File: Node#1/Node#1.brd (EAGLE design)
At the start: 100 x 80 mm, 110 parts, among them U1 BLUENRG-232, U2 SEMTECH_SX1503I091TRTSEMTECH_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, U3 MIC4468YWM, U4 LM339ADR, X1 2081-1228, X2 2081-1228, X3 2081-1228, Y1 ECS-160-12-36-AGN-TR, Y2 NX2012SA-32.768K-STD-MUB-1

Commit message: Update LBR
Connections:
- removed net N$83: X3.L2, X3.L4, X3.L6, X3.L8
- new net AGND: U$1.3, U$2.3, U$7.3, U$8.3, U3.7
- new net V+: U3.14, X3.L2, X3.L4, X3.L6, X3.L8
- net GND: no longer U$1.3, U$2.3, U$7.3, U$8.3, U3.7
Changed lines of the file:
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@@
 <contactref element="LED16" pad="K"/>
 <contactref element="D9" pad="3"/>
-<contactref element="U3" pad="7"/>
-<contactref element="U$1" pad="3"/>
-<contactref element="U$8" pad="3"/>
-<contactref element="U$7" pad="3"/>
-<contactref element="U$2" pad="3"/>
 <wire x1="-65.475" y1="-181.54" x2="-63.5" y2="-180.34" width="0" layer="19" extent="1-1"/>
 <wire x1="-61.525" y1="-181.54" x2="-63.5" y2="-180.34" width="0" layer="19" extent="1-1"/>
@@
 <wire x1="-17.78" y1="5.08" x2="-18.05" y2="-2.54" width="0" layer="19" extent="1-1"/>
 <wire x1="-19.03" y1="7.515" x2="-17.78" y2="5.08" width="0" layer="19" extent="1-1"/>
-<wire x1="4.4196" y1="4.0386" x2="-17.78" y2="5.08" width="0" layer="19" extent="1-1"/>
 <wire x1="-115.57" y1="-186.69" x2="-65.475" y2="-181.54" width="0" layer="19" extent="1-1"/>
 <wire x1="-116.84" y1="-227.5" x2="-115.57" y2="-186.69" width="0" layer="19" extent="1-1"/>
@@
 <wire x1="-115.57" y1="-372.11" x2="-115.57" y2="-377.19" width="0" layer="19" extent="1-1"/>
 <wire x1="-116.84" y1="-364.66" x2="-115.57" y2="-372.11" width="0" layer="19" extent="1-1"/>
-<wire x1="-149.42" y1="-404.495" x2="-115.57" y2="-377.19" width="0" layer="19" extent="1-1"/>
-<wire x1="-160.6804" y1="-408.7114" x2="-149.42" y2="-404.495" width="0" layer="19" extent="1-1"/>
-<wire x1="-173.3804" y1="-420.1414" x2="-160.6804" y2="-408.7114" width="0" layer="19" extent="1-1"/>
-<wire x1="-186.0804" y1="-432.8414" x2="-173.3804" y2="-420.1414" width="0" layer="19" extent="1-1"/>
 </signal>
 <signal name="N$12">
@@
 <wire x1="-160.6804" y1="-406.4" x2="-114.07" y2="-342.42" width="0" layer="19" extent="1-1"/>
 </signal>
-<signal name="N$83">
+<signal name="VCC">
+<contactref element="U4" pad="3"/>
+</signal>
+<signal name="V+">
 <contactref element="X3" pad="L2"/>
 <contactref element="X3" pad="L8"/>
 <contactref element="X3" pad="L6"/>
 <contactref element="X3" pad="L4"/>
+<contactref element="U3" pad="14"/>
 <wire x1="-107.07" y1="-345.92" x2="-107.07" y2="-352.92" width="0" layer="19" extent="1-1"/>
 <wire x1="-107.07" y1="-338.92" x2="-107.07" y2="-345.92" width="0" layer="19" extent="1-1"/>
 <wire x1="-107.07" y1="-331.92" x2="-107.07" y2="-338.92" width="0" layer="19" extent="1-1"/>
-</signal>
-<signal name="VCC">
-<contactref element="U4" pad="3"/>
+<wire x1="-140.14" y1="-399.415" x2="-107.07" y2="-352.92" width="0" layer="19" extent="1-1"/>
+</signal>
+<signal name="AGND">
+<contactref element="U3" pad="7"/>
+<contactref element="U$1" pad="3"/>
+<contactref element="U$8" pad="3"/>
+<contactref element="U$7" pad="3"/>
+<contactref element="U$2" pad="3"/>
+<wire x1="-173.3804" y1="-420.1414" x2="-186.0804" y2="-432.8414" width="0" layer="19" extent="1-1"/>
+<wire x1="-160.6804" y1="-408.7114" x2="-173.3804" y2="-420.1414" width="0" layer="19" extent="1-1"/>
+<wire x1="-149.42" y1="-404.495" x2="-160.6804" y2="-408.7114" width="0" layer="19" extent="1-1"/>
+<wire x1="4.4196" y1="4.0386" x2="-149.42" y2="-404.495" width="0" layer="19" extent="1-1"/>
 </signal>
 </signals>

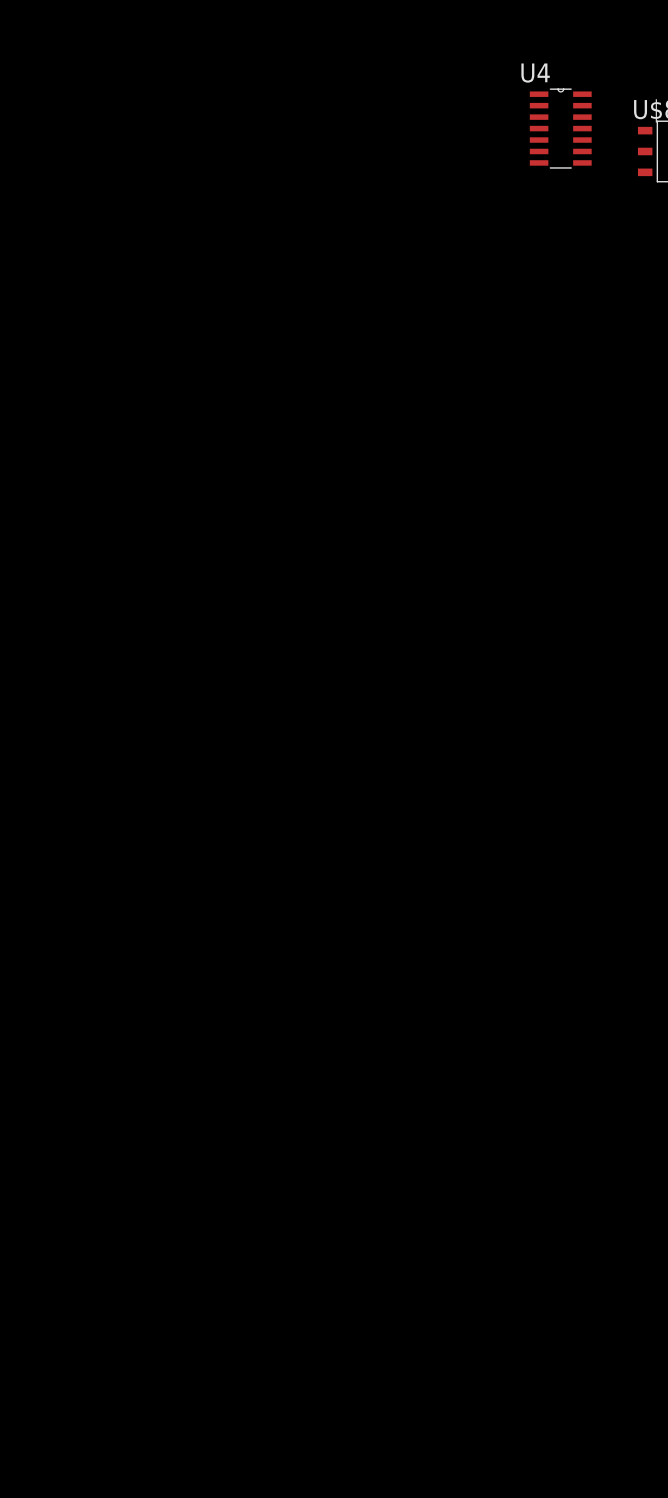
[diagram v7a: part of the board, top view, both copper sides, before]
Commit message: Update Endstufe Absicherung
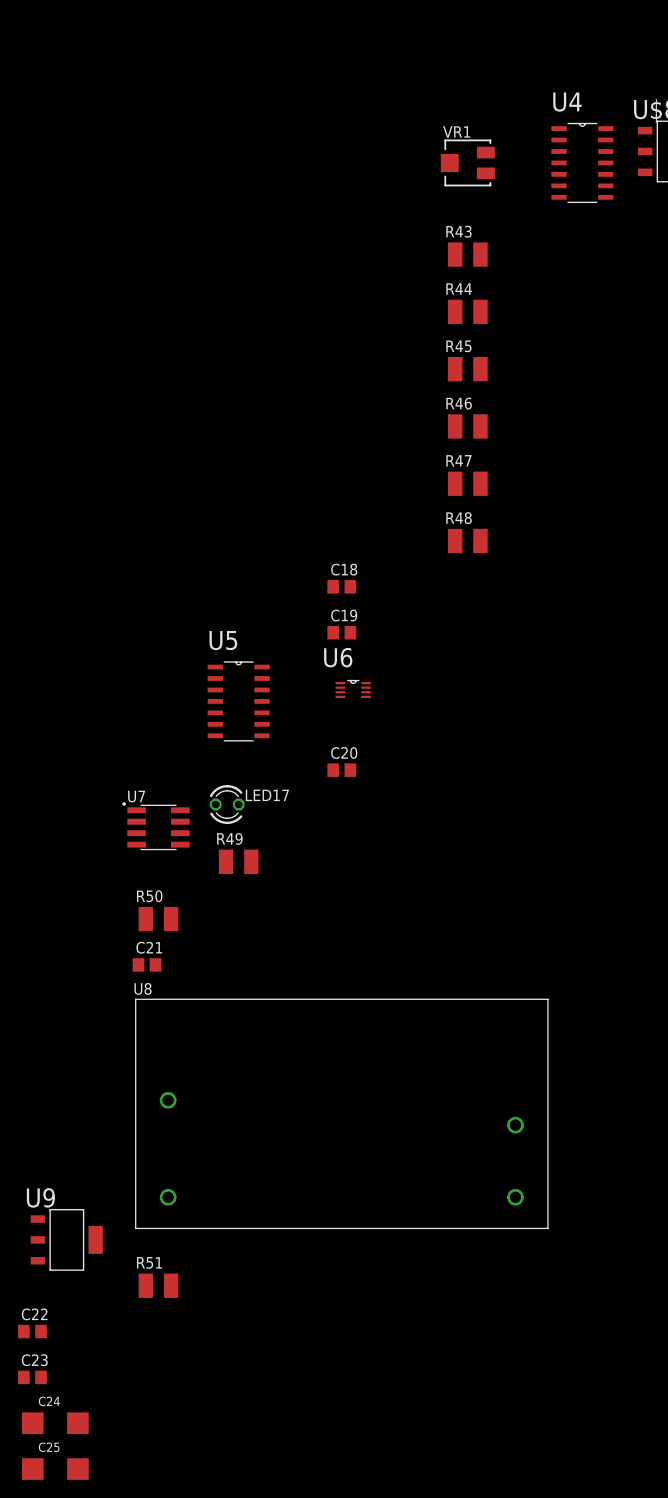
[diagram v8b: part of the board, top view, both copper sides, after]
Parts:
- added C18, C19, C20, C21, C22, C23: (no value), rcl:C0805
- added C24, C25: (no value), rcl:SMC_C
- added LED17: (no value), led:LED3MM
- added R43, R44, R45, R46, R47, R48, R49, R50, R51: (no value), rcl:R1210
- added U5: 74HC08D,652, BlueHome:SOIC127P600X175-14N
- added U6: SN74LVC1G74DCUR, BlueHome:SOP50P310X90-8N
- added U7: TMP75BID, BlueHome:SOIC127P600X175-8N
- added U8: IRM-05-5, BlueHome:CONV_IRM-05-5
- added U9: LMS8117AMP-3.3, BlueHome:SOT230P696X180-4N
- added VR1: TS53YJ103MR10, BlueHome:TRIM_TS53YJ103MR10
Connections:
- removed net VCC: U4.3
- new net ERROR: R49.1, U3.2, U3.4, U3.6, U3.9, U5.11
- new net E_RESET: U6.1
- new net N$100: X3.L2, X3.L4, X3.L6, X3.L8
- new net N$82: R43.1, VR1.C
- new net N$83: R43.2, R44.1, U4.11, U4.5, U4.7, U4.9
- new net N$84: R45.2, U4.6
- new net N$85: U4.1, U5.1
- new net N$86: R48.2, U4.10
- new net N$87: R47.2, U4.8
- new net N$88: R46.2, U4.4
- new net N$89: U4.2, U5.2
- new net N$90: U4.13, U5.4
- new net N$91: U4.14, U5.5
- new net N$92: U5.3, U5.9
- new net N$93: U5.10, U5.6
- new net N$94: U5.8, U6.6
- new net N$95: U8.AC/L
- new net N$96: U5.13, U6.5
- new net N$97: R50.1, U5.12, U7.3
- new net N$98: U8.AC/N
- net +3V3: now also C18.2, C19.1, C20.2, C21.2, C23.1, C25.+, LED17.A, R50.2, U4.3, U5.14, U6.2, U6.7, U6.8, U7.8, U9.2, U9.4
- net +5V: now also C22.1, C24.+, U8.VPOS, U9.3
- net AGND: now also R51.1, VR1.A, VR1.B
- net GND: now also C18.1, C19.2, C20.1, C21.1, C22.2, C23.2, C24.-, C25.-, R51.2, U4.12, U5.7, U6.4, U7.4, U7.5, U7.6, U7.7, U8.VNEG, U9.1, X2.L1, X2.L2, X2.L3, X2.L4, X2.L5, X2.L6, X2.L7, X2.L8
- net N$44: now also LED17.K, R49.2; no longer U3.2, U3.4, U3.6, U3.9
- net N$78: now also R45.1
- net N$79: now also R48.1
- net N$80: now also R47.1
- net N$81: now also R46.1
- net SCL: now also U7.2
- net SDA: now also U7.1
- net V+: now also R44.2; no longer X3.L2, X3.L4, X3.L6, X3.L8
